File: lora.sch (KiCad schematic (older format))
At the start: 1 part, among them U1 SX1301

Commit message: partialy wired - sequential pins
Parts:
- added C1: 1uF, symbol Device:CP
- added C2, C3, C4, C6: 100nF, Capacitor_SMD:C_0603_1608Metric_Pad1.05x0.95mm_HandSolder, symbol Device:C
- added C5, C7: 100n, Capacitor_SMD:C_0603_1608Metric_Pad1.05x0.95mm_HandSolder, symbol Device:C
- added C8: 1u, symbol Device:CP
- added J1: Conn_01x10_Male, Connector_PinHeader_2.54mm:PinHeader_1x10_P2.54mm_Vertical, symbol Connector:Conn_01x10_Male
- added J2: Conn_Coaxial, symbol Connector:Conn_Coaxial
- added R1, R2: 10k, Resistor_SMD:R_0603_1608Metric_Pad1.05x0.95mm_HandSolder, symbol Device:R
- added R10, R3, R4, R6, R7, R8, R9: 100, Resistor_SMD:R_0603_1608Metric_Pad1.05x0.95mm_HandSolder, symbol Device:R
- added R5: R, Resistor_SMD:R_0603_1608Metric_Pad1.05x0.95mm_HandSolder, symbol Device:R
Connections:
- net labels added: +1V8, +3V3, CS, LA_CTR, LB_CTR, MISO, MOSI, PA_CTR, PA_G0, PA_G1, PB_CTR, RA_EN, RB_CS, RB_EN, RB_MI, RB_MO, RB_SCK, RESET, R_RST, SCK
- wire segments 22 -> 109

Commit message: v1.0
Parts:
- added C10: 2n2, Capacitor_SMD:C_0402_1005Metric, symbol Device:C
- added C11: 22u, Capacitor_SMD:C_0603_1608Metric, symbol Device:CP
- added C12: 100nF, Capacitor_SMD:C_0402_1005Metric, symbol Device:C
- added C9: 10u, Capacitor_SMD:C_0603_1608Metric, symbol Device:CP
- added D1, D2, D3, D4, D5: LED, LED_SMD:LED_0402_1005Metric, symbol Device:LED
- added J3: Conn_01x08_Male, Connector_PinHeader_2.54mm:PinHeader_1x08_P2.54mm_Vertical, symbol Connector:Conn_01x08_Male
- added J4: Conn_01x10_Male, Connector_PinHeader_2.54mm:PinHeader_1x10_P2.54mm_Vertical, symbol Connector:Conn_01x10_Male
- added J5: Conn_01x06_Male, Connector_PinHeader_2.54mm:PinHeader_1x06_P2.54mm_Vertical, symbol Connector:Conn_01x06_Male
- added L1: 2.2uH, Inductor_SMD:L_6.3x6.3_H3, symbol pspice:INDUCTOR
- added R11: 100k, Resistor_SMD:R_0402_1005Metric, symbol Device:R
- added R12: 100, Resistor_SMD:R_0402_1005Metric, symbol Device:R
- added R13, R14, R15, R16, R17: 470, Resistor_SMD:R_0402_1005Metric, symbol Device:R
- added R18: 0, Resistor_SMD:R_0402_1005Metric, symbol Device:R
- added TP1, TP3: TestPoint, TestPoint:TestPoint_THTPad_1.5x1.5mm_Drill0.7mm, symbol Connector:TestPoint
- added U2: TPS62141, Package_DFN_QFN:QFN-16-1EP_3x3mm_P0.5mm_EP1.8x1.8mm, symbol Regulator_Switching:TPS62141
- added X1: DFA-S15, Oscillator:Oscillator_SMD_Fordahl_DFAS15-4Pin_5.0x3.2mm, symbol Oscillator:DFA-S15
- added X2: ASE-xxxMHz, Oscillator:Oscillator_SMD_Abracon_ASE-4Pin_3.2x2.5mm, symbol Oscillator:ASE-xxxMHz
- C1, C8: footprint (none) -> Capacitor_SMD:C_0603_1608Metric
- C2, C3, C4, C5, C6, C7: footprint Capacitor_SMD:C_0603_1608Metric_Pad1.05x0.95mm_HandSolder -> Capacitor_SMD:C_0402_1005Metric
- J2: footprint (none) -> Connector_Coaxial:U.FL_Molex_MCRF_73412-0110_Vertical
- R1, R10, R2, R3, R4, R6, R7, R8, R9: footprint Resistor_SMD:R_0603_1608Metric_Pad1.05x0.95mm_HandSolder -> Resistor_SMD:R_0402_1005Metric
- R5: value R -> 100; footprint Resistor_SMD:R_0603_1608Metric_Pad1.05x0.95mm_HandSolder -> Resistor_SMD:R_0402_1005Metric
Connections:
- net labels removed: LB_CTR, PB_CTR, RB_CS, RB_EN, RB_MI, RB_MO, RB_SCK, R_RST
- wire segments 109 -> 203
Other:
- moved on the sheet: C1, C2, C3, C4, C5, C6, C7, C8, J2, R1, R10, R2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

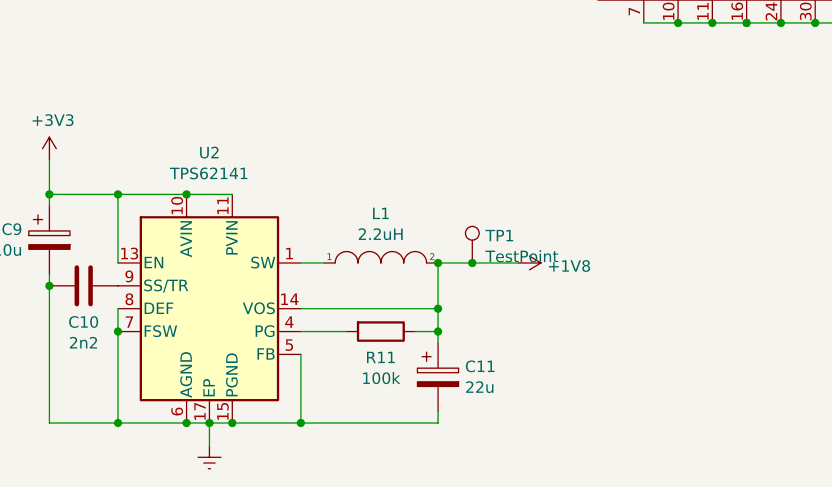
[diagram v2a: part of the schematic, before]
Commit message: replaced TPS62141 by TPS62140
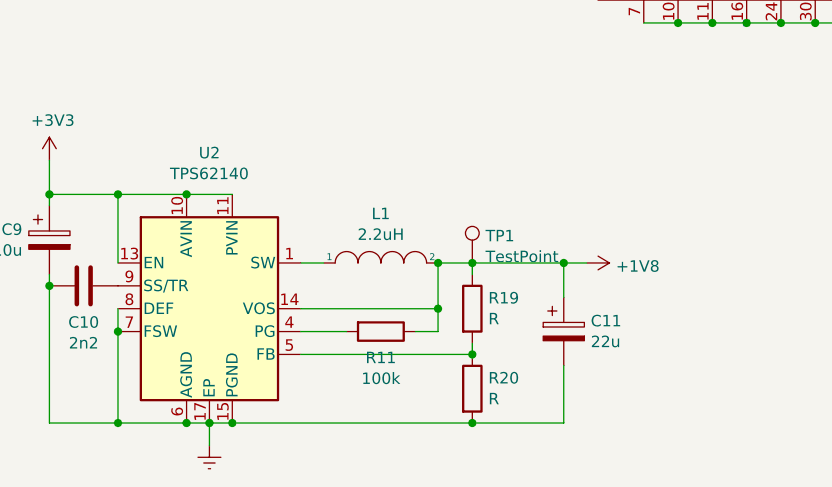
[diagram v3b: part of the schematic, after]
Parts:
- removed U2: TPS62141, Package_DFN_QFN:QFN-16-1EP_3x3mm_P0.5mm_EP1.8x1.8mm, symbol Regulator_Switching:TPS62141
- added R19, R20: R, Resistor_SMD:R_0402_1005Metric, symbol Device:R
- added U2: TPS62140, Package_DFN_QFN:VQFN-16-1EP_3x3mm_P0.5mm_EP1.68x1.68mm_ThermalVias, symbol Regulator_Switching:TPS62140
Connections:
- net +1V8: now also R19.1, U2.14 (VOS)
- net +3V3: now also U2.10 (AVIN), U2.11 (PVIN), U2.12 (PVIN), U2.13 (EN)
- net Earth: now also R20.2, U2.15 (PGND), U2.16 (PGND), U2.17 (EP), U2.6 (AGND), U2.7 (FSW), U2.8 (DEF)
- net at L1.1: now also U2.1 (SW), U2.2 (SW), U2.3 (SW)
- net at R11.2: now also U2.4 (PG)
- net at C10.1: now also U2.9 (SS/TR)
- new net: R19.2, R20.1, U2.5 (FB)
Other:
- moved on the sheet: C11
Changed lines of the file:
@@
 	1    0    0    -1
 $EndComp
-$Comp
-L Regulator_Switching:TPS62141 U2
-U 1 1 5DA22CC6
-P 2800 6450
-F 0 "U2" H 2800 7131 50  0000 C CNN
-F 1 "TPS62141" H 2800 7040 50  0000 C CNN
-F 2 "Package_DFN_QFN:QFN-16-1EP_3x3mm_P0.5mm_EP1.8x1.8mm" H 2950 6000 50  0001 L CNN
-F 3 "http://www.ti.com/lit/ds/symlink/TPS62140.pdf" H 2800 6450 50  0001 C CNN
-	1    2800 6450
-	1    0    0    -1
-$EndComp
-Wire Wire Line
-	2900 5950 2700 5950
 Wire Wire Line
 	2400 5950 2400 6250
-Connection ~ 2700 5950
-Wire Wire Line
-	2700 5950 2400 5950
 $Comp
 L power:+3V3 #PWR0107
@@
 	2100 5950 2400 5950
 Connection ~ 2400 5950
-Wire Wire Line
-	2900 6950 3200 6950
-Wire Wire Line
-	3200 6950 3200 6650
-Wire Wire Line
-	2900 6950 2800 6950
-Connection ~ 2900 6950
 Connection ~ 2800 6950
-Wire Wire Line
-	2800 6950 2700 6950
-Wire Wire Line
-	2400 6450 2400 6550
-Wire Wire Line
-	2400 6950 2700 6950
-Connection ~ 2400 6550
-Wire Wire Line
-	2400 6550 2400 6950
-Connection ~ 2700 6950
 $Comp
 L pspice:INDUCTOR L1
@@
 L Device:CP C11
 U 1 1 5DAA5D8F
-P 3800 6750
-F 0 "C11" H 3918 6796 50  0000 L CNN
-F 1 "22u" H 3918 6705 50  0000 L CNN
-F 2 "Capacitor_SMD:C_0603_1608Metric" H 3838 6600 50  0001 C CNN
-F 3 "~" H 3800 6750 50  0001 C CNN
-	1    3800 6750
+P 4350 6550
+F 0 "C11" H 4468 6596 50  0000 L CNN
+F 1 "22u" H 4468 6505 50  0000 L CNN
+F 2 "Capacitor_SMD:C_0603_1608Metric" H 4388 6400 50  0001 C CNN
+F 3 "~" H 4350 6550 50  0001 C CNN
+	1    4350 6550
 	1    0    0    -1
 $EndComp
@@
 L power:+1V8 #PWR0109
 U 1 1 5DAD42D4
-P 4150 6250
-F 0 "#PWR0109" H 4150 6100 50  0001 C CNN
-F 1 "+1V8" V 4165 6378 50  0000 L CNN
-F 2 "" H 4150 6250 50  0001 C CNN
-F 3 "" H 4150 6250 50  0001 C CNN
-	1    4150 6250
+P 4450 6250
+F 0 "#PWR0109" H 4450 6100 50  0001 C CNN
+F 1 "+1V8" V 4465 6378 50  0000 L CNN
+F 2 "" H 4450 6250 50  0001 C CNN
+F 3 "" H 4450 6250 50  0001 C CNN
+	1    4450 6250
 	0    1    1    0
 $EndComp
@@
 	2100 6000 2100 5950
 Connection ~ 2100 5950
-Wire Wire Line
-	3800 6600 3800 6550
-Connection ~ 3800 6550
-Wire Wire Line
-	3200 6950 3800 6950
-Wire Wire Line
-	3800 6950 3800 6900
-Connection ~ 3200 6950
 $Comp
 L power:Earth #PWR0111
@@
 $EndComp
 Connection ~ 3950 6250
-Wire Wire Line
-	3950 6250 4150 6250
 $Comp
 L Connector:Conn_01x10_Male J4
@@
 	7350 5200 7100 5200
 Connection ~ 7100 5200
+$Comp
+L Regulator_Switching:TPS62140 U2
+U 1 1 5DCB5A82
+P 2800 6450
+F 0 "U2" H 2800 7131 50  0000 C CNN
+F 1 "TPS62140" H 2800 7040 50  0000 C CNN
+F 2 "Package_DFN_QFN:VQFN-16-1EP_3x3mm_P0.5mm_EP1.68x1.68mm_ThermalVias" H 2950 6000 50  0001 L CNN
+F 3 "http://www.ti.com/lit/ds/symlink/TPS62140.pdf" H 2800 6450 50  0001 C CNN
+	1    2800 6450
+	1    0    0    -1
+$EndComp
+Wire Wire Line
+	2400 6450 2400 6550
+Wire Wire Line
+	2400 6550 2400 6950
+Connection ~ 2400 6550
+Wire Wire Line
+	2800 6950 2700 6950
+Wire Wire Line
+	2400 6950 2700 6950
+Connection ~ 2700 6950
+Wire Wire Line
+	2900 6950 2800 6950
+Connection ~ 2900 6950
+Wire Wire Line
+	2900 5950 2700 5950
+Wire Wire Line
+	2700 5950 2400 5950
+Connection ~ 2700 5950
+Wire Wire Line
+	4350 6400 4350 6250
+Connection ~ 4350 6250
+Wire Wire Line
+	4350 6250 4450 6250
+Wire Wire Line
+	3950 6250 4350 6250
+Wire Wire Line
+	4350 6950 4350 6700
+$Comp
+L Device:R R19
+U 1 1 5DD0E54E
+P 3950 6450
+F 0 "R19" H 4020 6496 50  0000 L CNN
+F 1 "R" H 4020 6405 50  0000 L CNN
+F 2 "Resistor_SMD:R_0402_1005Metric" V 3880 6450 50  0001 C CNN
+F 3 "~" H 3950 6450 50  0001 C CNN
+	1    3950 6450
+	1    0    0    -1
+$EndComp
+$Comp
+L Device:R R20
+U 1 1 5DD0EEC4
+P 3950 6800
+F 0 "R20" H 4020 6846 50  0000 L CNN
+F 1 "R" H 4020 6755 50  0000 L CNN
+F 2 "Resistor_SMD:R_0402_1005Metric" V 3880 6800 50  0001 C CNN
+F 3 "~" H 3950 6800 50  0001 C CNN
+	1    3950 6800
+	1    0    0    -1
+$EndComp
+Connection ~ 3950 6950
+Wire Wire Line
+	3950 6950 4350 6950
+Wire Wire Line
+	3950 6300 3950 6250
+Wire Wire Line
+	3950 6650 3950 6600
+Wire Wire Line
+	2900 6950 3950 6950
+Wire Wire Line
+	3200 6650 3950 6650
+Connection ~ 3950 6650
 $EndSCHEMATC

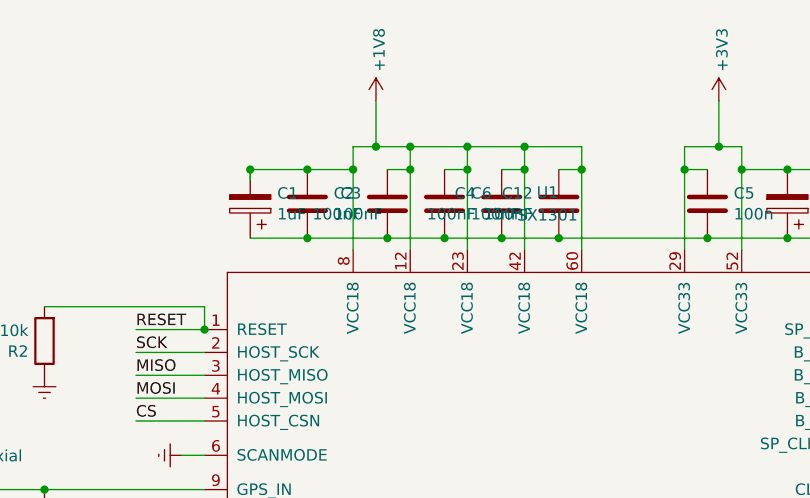
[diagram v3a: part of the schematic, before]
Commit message: updated pcb TPS, values harmonization
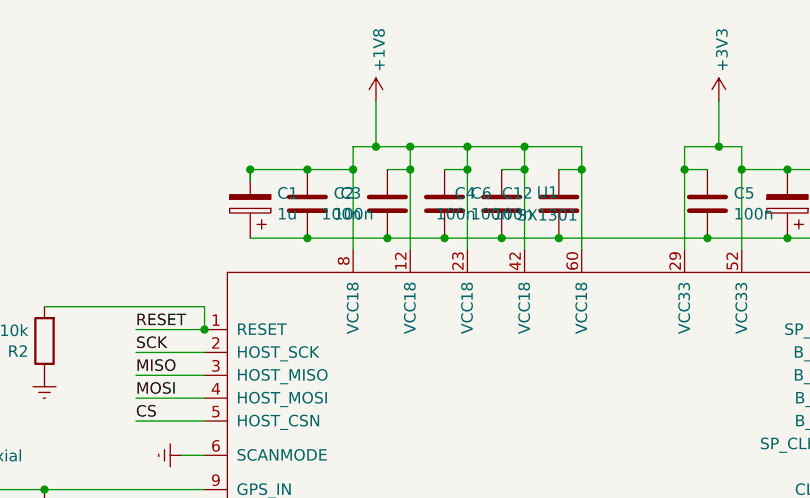
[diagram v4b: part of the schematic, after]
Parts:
- C1: value 1uF -> 1u
- C12, C2, C3, C4, C6: value 100nF -> 100n
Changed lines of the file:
@@
 P 4850 2000
 F 0 "C2" H 4965 2046 50  0000 L CNN
-F 1 "100nF" H 4965 1955 50  0000 L CNN
+F 1 "100n" H 4965 1955 50  0000 L CNN
 F 2 "Capacitor_SMD:C_0402_1005Metric" H 4888 1850 50  0001 C CNN
 F 3 "~" H 4850 2000 50  0001 C CNN
@@
 P 4600 2000
 F 0 "C1" H 4482 1954 50  0000 R CNN
-F 1 "1uF" H 4482 2045 50  0000 R CNN
+F 1 "1u" H 4482 2045 50  0000 R CNN
 F 2 "Capacitor_SMD:C_0603_1608Metric" H 4638 1850 50  0001 C CNN
 F 3 "~" H 4600 2000 50  0001 C CNN
@@
 P 5200 2000
 F 0 "C3" H 5086 2046 50  0000 R CNN
-F 1 "100nF" H 5086 1955 50  0000 R CNN
+F 1 "100n" H 5086 1955 50  0000 R CNN
 F 2 "Capacitor_SMD:C_0402_1005Metric" H 5238 1850 50  0001 C CNN
 F 3 "~" H 5200 2000 50  0001 C CNN
@@
 P 5700 2000
 F 0 "C4" H 5586 2046 50  0000 R CNN
-F 1 "100nF" H 5586 1955 50  0000 R CNN
+F 1 "100n" H 5586 1955 50  0000 R CNN
 F 2 "Capacitor_SMD:C_0402_1005Metric" H 5738 1850 50  0001 C CNN
 F 3 "~" H 5700 2000 50  0001 C CNN
@@
 P 5450 2000
 F 0 "C6" H 5565 2046 50  0000 L CNN
-F 1 "100nF" H 5565 1955 50  0000 L CNN
+F 1 "100n" H 5565 1955 50  0000 L CNN
 F 2 "Capacitor_SMD:C_0402_1005Metric" H 5488 1850 50  0001 C CNN
 F 3 "~" H 5450 2000 50  0001 C CNN
@@
 P 5950 2000
 F 0 "C12" H 5836 2046 50  0000 R CNN
-F 1 "100nF" H 5836 1955 50  0000 R CNN
+F 1 "100n" H 5836 1955 50  0000 R CNN
 F 2 "Capacitor_SMD:C_0402_1005Metric" H 5988 1850 50  0001 C CNN
 F 3 "~" H 5950 2000 50  0001 C CNN

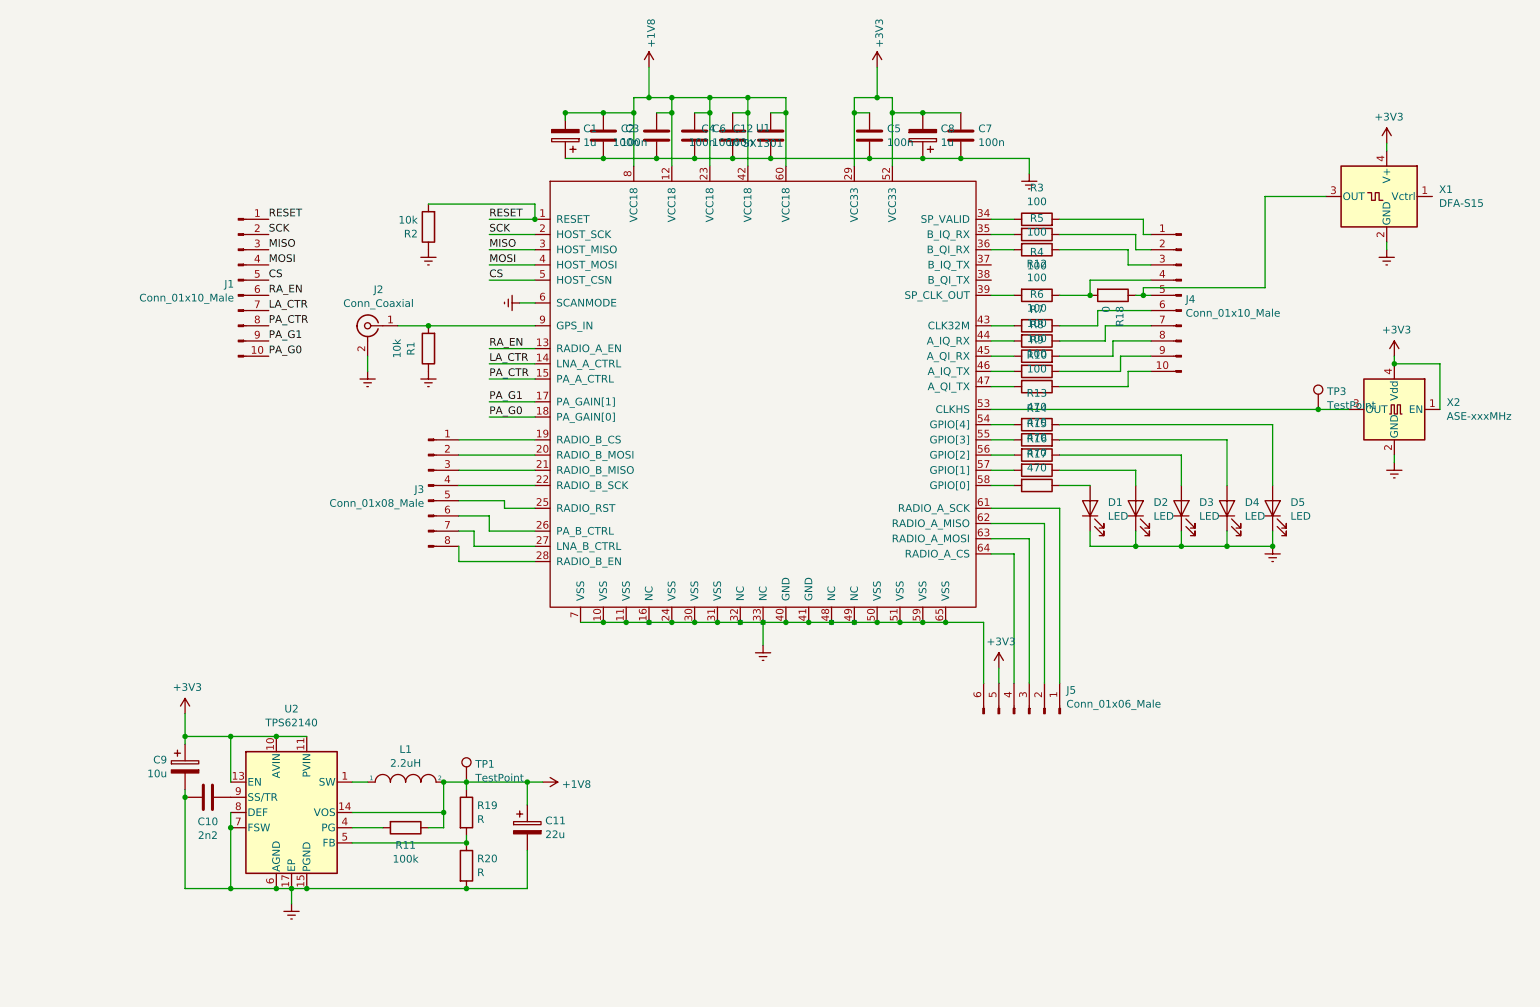
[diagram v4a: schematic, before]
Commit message: two regulators, old connectors removed
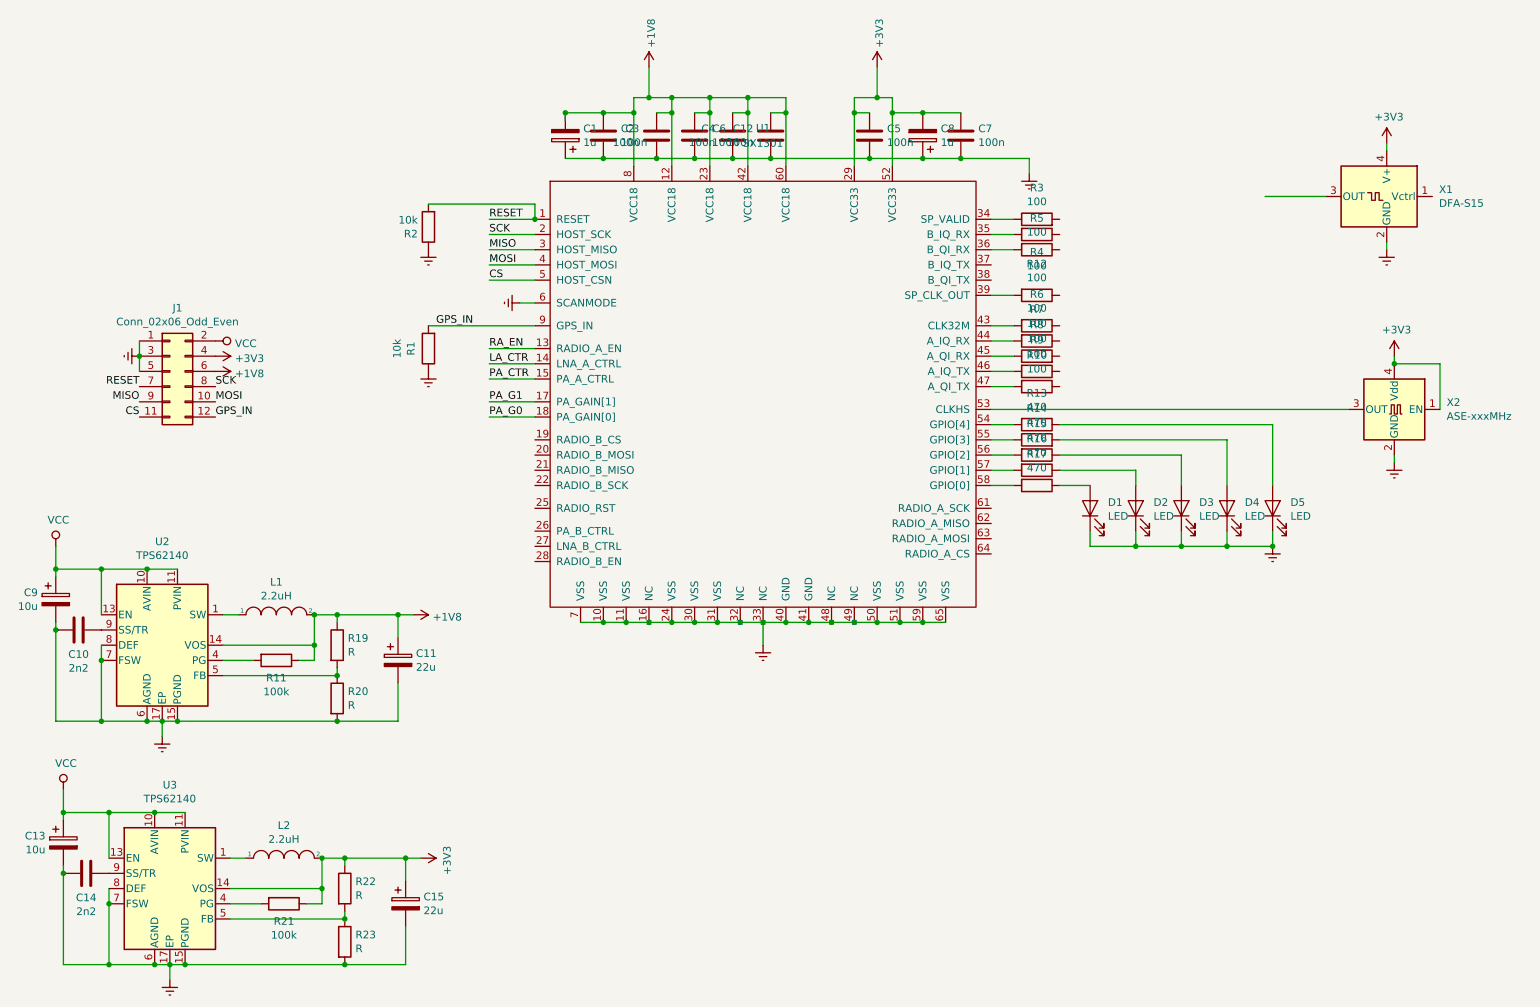
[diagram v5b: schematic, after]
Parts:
- removed J1, J4: Conn_01x10_Male, Connector_PinHeader_2.54mm:PinHeader_1x10_P2.54mm_Vertical, symbol Connector:Conn_01x10_Male
- removed J2: Conn_Coaxial, Connector_Coaxial:U.FL_Molex_MCRF_73412-0110_Vertical, symbol Connector:Conn_Coaxial
- removed J3: Conn_01x08_Male, Connector_PinHeader_2.54mm:PinHeader_1x08_P2.54mm_Vertical, symbol Connector:Conn_01x08_Male
- removed J5: Conn_01x06_Male, Connector_PinHeader_2.54mm:PinHeader_1x06_P2.54mm_Vertical, symbol Connector:Conn_01x06_Male
- removed R18: 0, Resistor_SMD:R_0402_1005Metric, symbol Device:R
- removed TP1, TP3: TestPoint, TestPoint:TestPoint_THTPad_1.5x1.5mm_Drill0.7mm, symbol Connector:TestPoint
- added C13: 10u, Capacitor_SMD:C_0603_1608Metric, symbol Device:CP
- added C14: 2n2, Capacitor_SMD:C_0402_1005Metric, symbol Device:C
- added C15: 22u, Capacitor_SMD:C_0603_1608Metric, symbol Device:CP
- added J1: Conn_02x06_Odd_Even, Connector_PinHeader_2.54mm:PinHeader_2x06_P2.54mm_Vertical, symbol Connector_Generic:Conn_02x06_Odd_Even
- added L2: 2.2uH, Inductor_SMD:L_6.3x6.3_H3, symbol pspice:INDUCTOR
- added R21: 100k, Resistor_SMD:R_0402_1005Metric, symbol Device:R
- added R22, R23: R, Resistor_SMD:R_0402_1005Metric, symbol Device:R
- added U3: TPS62140, Package_DFN_QFN:VQFN-16-1EP_3x3mm_P0.5mm_EP1.68x1.68mm_ThermalVias, symbol Regulator_Switching:TPS62140
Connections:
- net +1V8: now also J1.6 (Pin_6)
- net +3V3: now also C15.1, J1.4 (Pin_4), L2.2, R21.1, R22.1, U3.14 (VOS); no longer C9.1, U2.10 (AVIN), U2.11 (PVIN), U2.12 (PVIN), U2.13 (EN)
- net CS: now also J1.11 (Pin_11)
- net Earth: now also C13.2, C14.2, C15.2, J1.1 (Pin_1), J1.3 (Pin_3), J1.5 (Pin_5), R23.2, U3.15 (PGND), U3.16 (PGND), U3.17 (EP), U3.6 (AGND), U3.7 (FSW), U3.8 (DEF)
- net MISO: now also J1.9 (Pin_9)
- net MOSI: now also J1.10 (Pin_10)
- net RESET: now also J1.7 (Pin_7)
- net SCK: now also J1.8 (Pin_8)
- net GPS_IN: now reaches R1.2, U1.9 (GPS_IN)
- net GPS_IN: now also J1.12 (Pin_12)
- new net: L2.1, U3.1 (SW), U3.2 (SW), U3.3 (SW)
- new net: R21.2, U3.4 (PG)
- new net: C14.1, U3.9 (SS/TR)
- new net: R22.2, R23.1, U3.5 (FB)
- new net VCC: C13.1, C9.1, J1.2 (Pin_2), U2.10 (AVIN), U2.11 (PVIN), U2.12 (PVIN), U2.13 (EN), U3.10 (AVIN), U3.11 (PVIN), U3.12 (PVIN), U3.13 (EN)
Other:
- moved on the sheet: C10, C11, C9, L1, R11, R19, R20, U2
